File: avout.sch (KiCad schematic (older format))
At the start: 46 parts, among them CN6 AUDIO_VIDEO, M1 Modulator, Q3 2SC1815, Q81 BC547, Q82 BC547

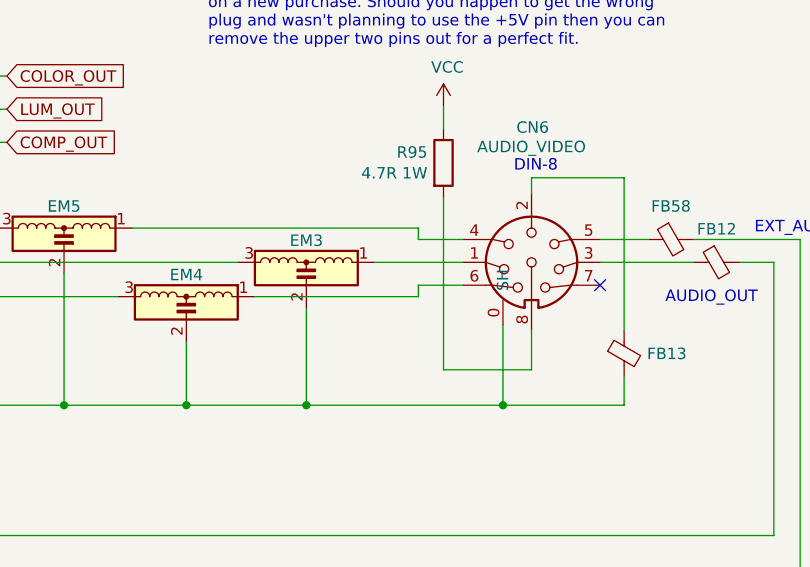
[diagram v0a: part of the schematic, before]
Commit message: Add ferrite on A/V power out
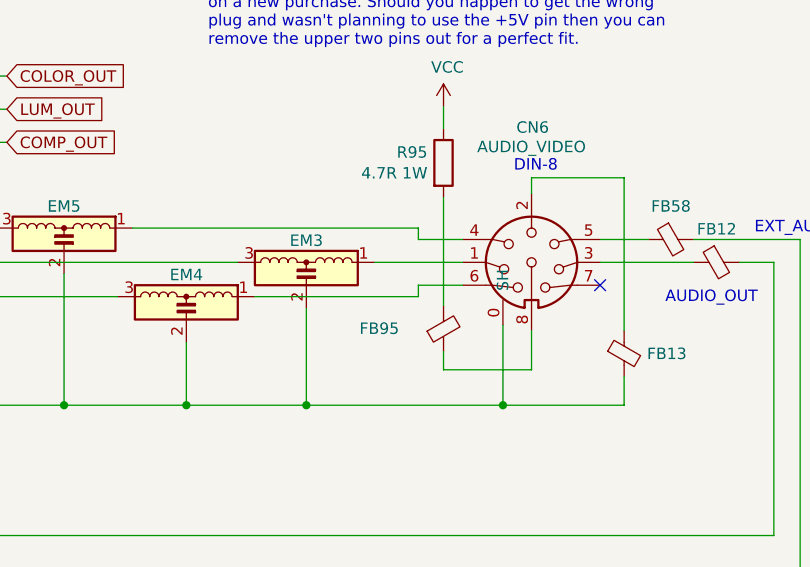
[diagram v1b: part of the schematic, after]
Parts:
- added FB95: Ferrite_Bead_Small, LittleSixteen:Ferrite, symbol Device:Ferrite_Bead_Small
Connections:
- net GND: now also FB95.3 (GND)
- net at R95.2: now also FB95.2; no longer CN6.8
- new net: CN6.8, FB95.1
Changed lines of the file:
@@
 Sheet 12 12
 Title "LittleSixteen"
-Date "2021-11-09"
+Date "2021-11-29"
 Rev "3git"
 Comp "SukkoPera"
@@
 	9645 2785 9260 2785
 Wire Wire Line
-	9260 2785 9260 2030
+	9260 2785 9260 2705
 $Comp
 L power:VCC #PWR0179
@@
 Wire Wire Line
 	9260 1730 9260 1635
+$Comp
+L Device:Ferrite_Bead_Small FB95
+U 1 1 61E4B6DF
+P 9260 2605
+F 0 "FB95" H 9066 2605 50  0000 R CNN
+F 1 "Ferrite_Bead_Small" H 9360 2560 50  0001 L CNN
+F 2 "LittleSixteen:Ferrite" V 9190 2605 50  0001 C CNN
+F 3 "~" H 9260 2605 50  0001 C CNN
+	1    9260 2605
+	1    0    0    1
+$EndComp
+Wire Wire Line
+	9260 2505 9260 2030
 $EndSCHEMATC

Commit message: Various minor fixes
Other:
- note added: "ADDITIONAL CURRENT-\nLIMITING RESISTOR AND\nEMI-PROTECTION FERRITE"
- note removed: "OPTIONAL\nPULL-UP"
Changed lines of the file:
@@
 Wire Wire Line
 	7810 4935 7810 4860
-Text Notes 7180 4910 0    50   ~ 0
-OPTIONAL\nPULL-UP
 Wire Wire Line
 	3430 5395 3430 5760
@@
 Wire Wire Line
 	9260 2505 9260 2030
+Wire Notes Line
+	8825 1700 9350 1700
+Wire Notes Line
+	9350 1700 9350 2835
+Wire Notes Line
+	9350 2835 8825 2835
+Wire Notes Line
+	8825 2835 8825 1700
+Text Notes 9285 3260 2    50   ~ 0
+ADDITIONAL CURRENT-\nLIMITING RESISTOR AND\nEMI-PROTECTION FERRITE
 $EndSCHEMATC

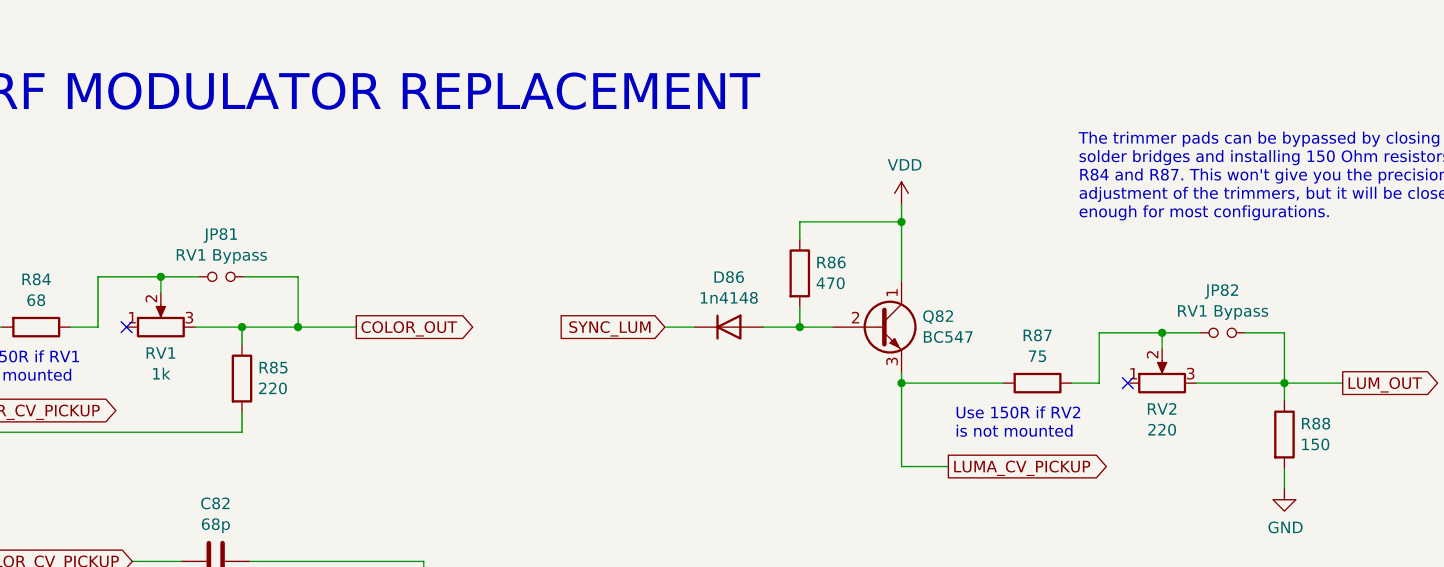
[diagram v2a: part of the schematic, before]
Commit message: Add jumper on RAMEN
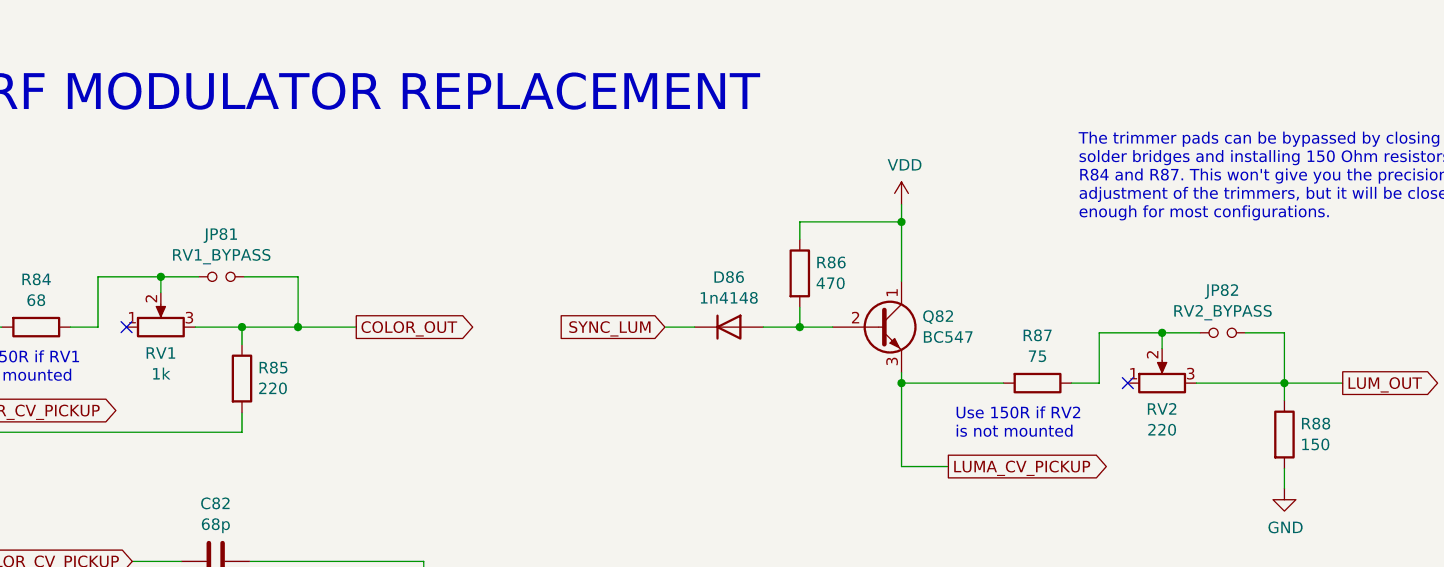
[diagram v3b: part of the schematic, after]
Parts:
- JP81: value RV1 Bypass -> RV1_BYPASS
- JP82: value RV1 Bypass -> RV2_BYPASS
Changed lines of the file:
@@
 P 4835 5175
 F 0 "JP81" H 4835 5360 50  0000 C CNN
-F 1 "RV1 Bypass" H 4835 5269 50  0000 C CNN
+F 1 "RV1_BYPASS" H 4835 5269 50  0000 C CNN
 F 2 "Jumper:SolderJumper-2_P1.3mm_Open_RoundedPad1.0x1.5mm" H 4835 5175 50  0001 C CNN
 F 3 "~" H 4835 5175 50  0001 C CNN
@@
 P 9215 5420
 F 0 "JP82" H 9215 5605 50  0000 C CNN
-F 1 "RV1 Bypass" H 9215 5514 50  0000 C CNN
+F 1 "RV2_BYPASS" H 9215 5514 50  0000 C CNN
 F 2 "Jumper:SolderJumper-2_P1.3mm_Open_RoundedPad1.0x1.5mm" H 9215 5420 50  0001 C CNN
 F 3 "~" H 9215 5420 50  0001 C CNN

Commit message: Use local Ferrite_Bead_Small symbol
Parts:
- FB12, FB13, FB58, FB95: symbol Device:Ferrite_Bead_Small -> ferrite_bead_small:Ferrite_Bead_Small
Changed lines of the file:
@@
 $EndComp
 $Comp
-L Device:Ferrite_Bead_Small FB13
+L ferrite_bead_small:Ferrite_Bead_Small FB13
 U 1 1 5E03E255
 P 10050 2715
@@
 	10050 2815 10050 2940
 $Comp
-L Device:Ferrite_Bead_Small FB12
+L ferrite_bead_small:Ferrite_Bead_Small FB12
 U 1 1 5E03F938
 P 10455 2315
@@
 $EndComp
 $Comp
-L Device:Ferrite_Bead_Small FB58
+L ferrite_bead_small:Ferrite_Bead_Small FB58
 U 1 1 5E040A9B
 P 10255 2215
@@
 	9260 1730 9260 1635
 $Comp
-L Device:Ferrite_Bead_Small FB95
+L ferrite_bead_small:Ferrite_Bead_Small FB95
 U 1 1 61E4B6DF
 P 9260 2605

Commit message: Use clearer diode footprint
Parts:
- D86: footprint Diode_THT:D_DO-35_SOD27_P5.08mm_Vertical_KathodeUp -> LittleSixteen:D_DO-35_SOD27_P5.08mm_Vertical_KathodeUp
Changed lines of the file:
@@
 F 0 "D86" H 7055 5612 50  0000 C CNN
 F 1 "1n4148" H 7055 5521 50  0000 C CNN
-F 2 "Diode_THT:D_DO-35_SOD27_P5.08mm_Vertical_KathodeUp" H 7055 5395 50  0001 C CNN
+F 2 "LittleSixteen:D_DO-35_SOD27_P5.08mm_Vertical_KathodeUp" H 7055 5395 50  0001 C CNN
 F 3 "~" H 7055 5395 50  0001 C CNN
 	1    7055 5395
